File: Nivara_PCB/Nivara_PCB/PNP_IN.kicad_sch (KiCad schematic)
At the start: 4 parts, among them U7 LTV-357T

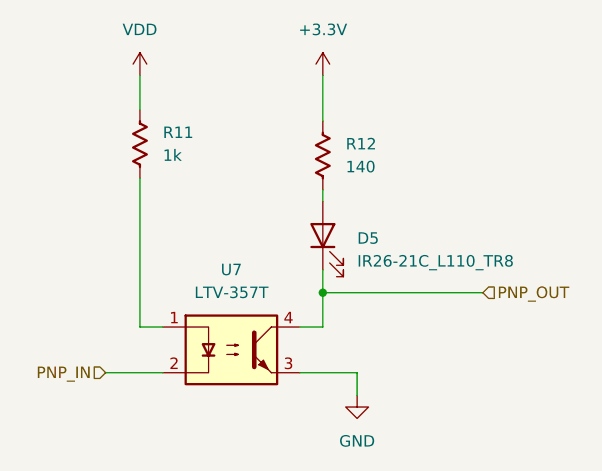
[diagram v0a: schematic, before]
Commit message: Cambios finales en la comprobación del DRC.
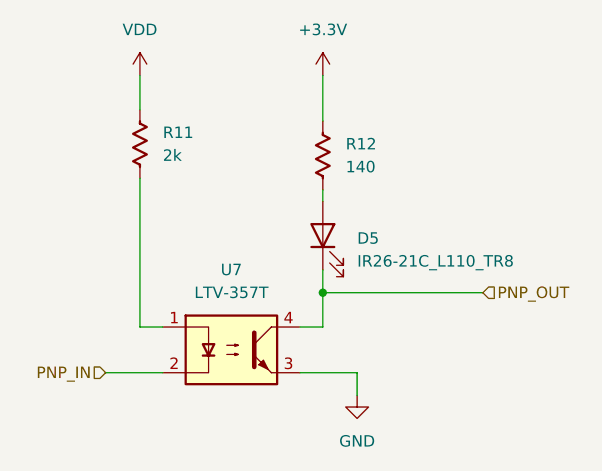
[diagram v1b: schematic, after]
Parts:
- R11: value 1k -> 2k
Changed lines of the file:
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@@
 			)
 		)
-		(property "Value" "1k"
+		(property "Value" "2k"
 			(at 83.82 76.1999 0)
 			(effects

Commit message: TERMINACIONES Y AJUSTES FINALES
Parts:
- removed D5: IR26-21C_L110_TR8, LED_SMD:LED_1206_3216Metric, symbol LED:IR26-21C_L110_TR8
- added D12: LED, LED_SMD:LED_0603_1608Metric, symbol EasyEDA:LED
- R15: renamed from R11; LCSC Part (none) -> C22975; Part # (none) -> 0603WAF2001T5E
- R16: renamed from R12; LCSC Part (none) -> C245910; Part # (none) -> RC0603FR-07140RL
- U9: renamed from U7; LCSC Part (none) -> C119091; Part # (none) -> LTV-357T-C
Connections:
- net PNP_OUT: now also D12.1 (K)
- net at R16.2: now also D12.2 (A)
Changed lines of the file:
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@@
-	)
-	(symbol
-		(lib_id "LED:IR26-21C_L110_TR8")
-		(at 101.6 85.09 90)
-		(unit 1)
-		(exclude_from_sim no)
-		(in_bom yes)
-		(on_board yes)
-		(dnp no)
-		(fields_autoplaced yes)
-		(property "Reference" "D5"
-			(at 105.41 85.4074 90)
-			(effects
-				(font
-					(size 1.27 1.27)
-				)
-				(justify right)
-			)
-		)
-		(property "Value" "IR26-21C_L110_TR8"
-			(at 105.41 87.9474 90)
-			(effects
-				(font
-					(size 1.27 1.27)
-				)
-				(justify right)
-			)
-		)
-		(property "Footprint" "LED_SMD:LED_1206_3216Metric"
-			(at 96.52 85.09 0)
-			(effects
-				(font
-					(size 1.27 1.27)
-				)
-				(hide yes)
-			)
-		)
-		(property "Datasheet" "http://www.everlight.com/file/ProductFile/IR26-21C-L110-TR8.pdf"
-			(at 101.6 85.09 0)
-			(effects
-				(font
-					(size 1.27 1.27)
-				)
-				(hide yes)
-			)
-		)
-		(property "Description" "940nm, 20 deg, Infrared LED, 1206"
-			(at 101.6 85.09 0)
-			(effects
-				(font
-					(size 1.27 1.27)
-				)
-				(hide yes)
-			)
-		)
-		(pin "2"
-		)
-		(pin "1"
-		)
-		(instances
-			(project "Nivara_PCB"
-				(path "/13184db0-a71d-4054-b13a-bbf46d2b100d/4e7fa7f2-8bf5-4f9c-874d-fa1b4fd76f92/48f5ac7a-6bba-49c0-99bb-db418c675091"
-					(reference "D5")
-					(unit 1)
-				)
-				(path "/13184db0-a71d-4054-b13a-bbf46d2b100d/4e7fa7f2-8bf5-4f9c-874d-fa1b4fd76f92/caca7181-9f66-4070-8ce1-bf0189ab573e"
-					(reference "D21")
-					(unit 1)
-				)
-			)
-		)
 	)
 	(symbol
@@
 		(dnp no)
 		(fields_autoplaced yes)
-		(property "Reference" "#PWR030"
+		(property "Reference" "#PWR034"
 			(at 101.6 71.12 0)
 			(effects
@@
 			(project "Nivara_PCB"
 				(path "/13184db0-a71d-4054-b13a-bbf46d2b100d/4e7fa7f2-8bf5-4f9c-874d-fa1b4fd76f92/48f5ac7a-6bba-49c0-99bb-db418c675091"
-					(reference "#PWR030")
-					(unit 1)
-				)
-				(path "/13184db0-a71d-4054-b13a-bbf46d2b100d/4e7fa7f2-8bf5-4f9c-874d-fa1b4fd76f92/caca7181-9f66-4070-8ce1-bf0189ab573e"
-					(reference "#PWR059")
+					(reference "#PWR034")
+					(unit 1)
+				)
+				(path "/13184db0-a71d-4054-b13a-bbf46d2b100d/4e7fa7f2-8bf5-4f9c-874d-fa1b4fd76f92/caca7181-9f66-4070-8ce1-bf0189ab573e"
+					(reference "#PWR062")
 					(unit 1)
 				)
@@
 		(dnp no)
 		(fields_autoplaced yes)
-		(property "Reference" "R12"
+		(property "Reference" "R16"
 			(at 104.14 74.9299 0)
 			(effects
@@
 			)
 		)
-		(property "Datasheet" "~"
+		(property "Datasheet" "https://www.lcsc.com/datasheet/C245910.pdf"
 			(at 101.6 76.2 0)
 			(effects
@@
 			)
 		)
+		(property "Part #" "RC0603FR-07140RL"
+			(at 101.6 76.2 0)
+			(effects
+				(font
+					(size 1.27 1.27)
+				)
+				(hide yes)
+			)
+		)
+		(property "LCSC Part" "C245910"
+			(at 101.6 76.2 0)
+			(effects
+				(font
+					(size 1.27 1.27)
+				)
+				(hide yes)
+			)
+		)
 		(pin "2"
 		)
@@
 			(project "Nivara_PCB"
 				(path "/13184db0-a71d-4054-b13a-bbf46d2b100d/4e7fa7f2-8bf5-4f9c-874d-fa1b4fd76f92/48f5ac7a-6bba-49c0-99bb-db418c675091"
-					(reference "R12")
-					(unit 1)
-				)
-				(path "/13184db0-a71d-4054-b13a-bbf46d2b100d/4e7fa7f2-8bf5-4f9c-874d-fa1b4fd76f92/caca7181-9f66-4070-8ce1-bf0189ab573e"
-					(reference "R36")
+					(reference "R16")
+					(unit 1)
+				)
+				(path "/13184db0-a71d-4054-b13a-bbf46d2b100d/4e7fa7f2-8bf5-4f9c-874d-fa1b4fd76f92/caca7181-9f66-4070-8ce1-bf0189ab573e"
+					(reference "R42")
 					(unit 1)
 				)
@@
 		(dnp no)
 		(fields_autoplaced yes)
-		(property "Reference" "#PWR086"
+		(property "Reference" "#PWR033"
 			(at 81.28 71.12 0)
 			(effects
@@
 			(project "Nivara_PCB"
 				(path "/13184db0-a71d-4054-b13a-bbf46d2b100d/4e7fa7f2-8bf5-4f9c-874d-fa1b4fd76f92/48f5ac7a-6bba-49c0-99bb-db418c675091"
-					(reference "#PWR086")
-					(unit 1)
-				)
-				(path "/13184db0-a71d-4054-b13a-bbf46d2b100d/4e7fa7f2-8bf5-4f9c-874d-fa1b4fd76f92/caca7181-9f66-4070-8ce1-bf0189ab573e"
-					(reference "#PWR058")
+					(reference "#PWR033")
+					(unit 1)
+				)
+				(path "/13184db0-a71d-4054-b13a-bbf46d2b100d/4e7fa7f2-8bf5-4f9c-874d-fa1b4fd76f92/caca7181-9f66-4070-8ce1-bf0189ab573e"
+					(reference "#PWR061")
 					(unit 1)
 				)
@@
 		(dnp no)
 		(fields_autoplaced yes)
-		(property "Reference" "U7"
+		(property "Reference" "U9"
 			(at 91.44 88.9 0)
 			(effects
@@
 			)
 		)
-		(property "Datasheet" "https://www.buerklin.com/medias/sys_master/download/download/h91/ha0/8892020588574.pdf"
+		(property "Datasheet" "https://www.lcsc.com/datasheet/C119091.pdf"
 			(at 91.44 97.79 0)
 			(effects
@@
 			)
 		)
+		(property "Part #" "LTV-357T-C"
+			(at 91.44 97.79 0)
+			(effects
+				(font
+					(size 1.27 1.27)
+				)
+				(hide yes)
+			)
+		)
+		(property "LCSC Part" "C119091"
+			(at 91.44 97.79 0)
+			(effects
+				(font
+					(size 1.27 1.27)
+				)
+				(hide yes)
+			)
+		)
 		(pin "3"
 		)
@@
 			(project "Nivara_PCB"
 				(path "/13184db0-a71d-4054-b13a-bbf46d2b100d/4e7fa7f2-8bf5-4f9c-874d-fa1b4fd76f92/48f5ac7a-6bba-49c0-99bb-db418c675091"
-					(reference "U7")
-					(unit 1)
-				)
-				(path "/13184db0-a71d-4054-b13a-bbf46d2b100d/4e7fa7f2-8bf5-4f9c-874d-fa1b4fd76f92/caca7181-9f66-4070-8ce1-bf0189ab573e"
-					(reference "U15")
+					(reference "U9")
+					(unit 1)
+				)
+				(path "/13184db0-a71d-4054-b13a-bbf46d2b100d/4e7fa7f2-8bf5-4f9c-874d-fa1b4fd76f92/caca7181-9f66-4070-8ce1-bf0189ab573e"
+					(reference "U17")
+					(unit 1)
+				)
+			)
+		)
+	)
+	(symbol
+		(lib_id "EasyEDA:LED")
+		(at 101.6 85.09 270)
+		(mirror x)
+		(unit 1)
+		(exclude_from_sim no)
+		(in_bom yes)
+		(on_board yes)
+		(dnp no)
+		(property "Reference" "D12"
+			(at 111.252 85.09 90)
+			(effects
+				(font
+					(size 1.27 1.27)
+				)
+				(justify right)
+			)
+		)
+		(property "Value" "LED"
+			(at 111.252 87.63 90)
+			(effects
+				(font
+					(size 1.27 1.27)
+				)
+				(justify right)
+			)
+		)
+		(property "Footprint" "LED_SMD:LED_0603_1608Metric"
+			(at 101.6 85.09 0)
+			(effects
+				(font
+					(size 1.27 1.27)
+				)
+				(hide yes)
+			)
+		)
+		(property "Datasheet" "https://www.lcsc.com/datasheet/C440520.pdf"
+			(at 101.6 85.09 0)
+			(effects
+				(font
+					(size 1.27 1.27)
+				)
+				(hide yes)
+			)
+		)
+		(property "Description" "Light emitting diode"
+			(at 101.6 85.09 0)
+			(effects
+				(font
+					(size 1.27 1.27)
+				)
+				(hide yes)
+			)
+		)
+		(property "Sim.Pins" "1=K 2=A"
+			(at 101.6 85.09 0)
+			(effects
+				(font
+					(size 1.27 1.27)
+				)
+				(hide yes)
+			)
+		)
+		(property "LCSC Part" "C12065"
+			(at 101.6 85.09 90)
+			(effects
+				(font
+					(size 1.27 1.27)
+				)
+				(hide yes)
+			)
+		)
+		(property "Part #" "LTST-C193TGKT-5A"
+			(at 101.6 85.09 90)
+			(effects
+				(font
+					(size 1.27 1.27)
+				)
+				(hide yes)
+			)
+		)
+		(pin "1"
+		)
+		(pin "2"
+		)
+		(instances
+			(project "Nivara_PCB"
+				(path "/13184db0-a71d-4054-b13a-bbf46d2b100d/4e7fa7f2-8bf5-4f9c-874d-fa1b4fd76f92/48f5ac7a-6bba-49c0-99bb-db418c675091"
+					(reference "D12")
+					(unit 1)
+				)
+				(path "/13184db0-a71d-4054-b13a-bbf46d2b100d/4e7fa7f2-8bf5-4f9c-874d-fa1b4fd76f92/caca7181-9f66-4070-8ce1-bf0189ab573e"
+					(reference "D27")
 					(unit 1)
 				)
@@
 		(dnp no)
 		(fields_autoplaced yes)
-		(property "Reference" "#PWR031"
+		(property "Reference" "#PWR035"
 			(at 105.41 109.22 0)
 			(effects
@@
 			(project "Nivara_PCB"
 				(path "/13184db0-a71d-4054-b13a-bbf46d2b100d/4e7fa7f2-8bf5-4f9c-874d-fa1b4fd76f92/48f5ac7a-6bba-49c0-99bb-db418c675091"
-					(reference "#PWR031")
-					(unit 1)
-				)
-				(path "/13184db0-a71d-4054-b13a-bbf46d2b100d/4e7fa7f2-8bf5-4f9c-874d-fa1b4fd76f92/caca7181-9f66-4070-8ce1-bf0189ab573e"
-					(reference "#PWR068")
+					(reference "#PWR035")
+					(unit 1)
+				)
+				(path "/13184db0-a71d-4054-b13a-bbf46d2b100d/4e7fa7f2-8bf5-4f9c-874d-fa1b4fd76f92/caca7181-9f66-4070-8ce1-bf0189ab573e"
+					(reference "#PWR063")
 					(unit 1)
 				)
@@
 		(dnp no)
 		(fields_autoplaced yes)
-		(property "Reference" "R11"
+		(property "Reference" "R15"
 			(at 83.82 73.6599 0)
 			(effects
@@
 			)
 		)
-		(property "Datasheet" "~"
+		(property "Datasheet" "https://jlcpcb.com/api/file/downloadByFileSystemAccessId/8579706189568917504"
 			(at 81.28 74.93 0)
 			(effects
@@
 			)
 		)
+		(property "Part #" "0603WAF2001T5E"
+			(at 81.28 74.93 0)
+			(effects
+				(font
+					(size 1.27 1.27)
+				)
+				(hide yes)
+			)
+		)
+		(property "LCSC Part" "C22975"
+			(at 81.28 74.93 0)
+			(effects
+				(font
+					(size 1.27 1.27)
+				)
+				(hide yes)
+			)
+		)
 		(pin "2"
 		)
@@
 			(project "Nivara_PCB"
 				(path "/13184db0-a71d-4054-b13a-bbf46d2b100d/4e7fa7f2-8bf5-4f9c-874d-fa1b4fd76f92/48f5ac7a-6bba-49c0-99bb-db418c675091"
-					(reference "R11")
-					(unit 1)
-				)
-				(path "/13184db0-a71d-4054-b13a-bbf46d2b100d/4e7fa7f2-8bf5-4f9c-874d-fa1b4fd76f92/caca7181-9f66-4070-8ce1-bf0189ab573e"
-					(reference "R35")
-					(unit 1)
-				)
+					(reference "R15")
+					(unit 1)
+				)
+				(path "/13184db0-a71d-4054-b13a-bbf46d2b100d/4e7fa7f2-8bf5-4f9c-874d-fa1b4fd76f92/caca7181-9f66-4070-8ce1-bf0189ab573e"
+					(reference "R41")
+					(unit 1)
+				)
